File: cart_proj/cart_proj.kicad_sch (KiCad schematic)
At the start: 11 parts, among them CON1 GENESIS-EDGE, J1 PAD3, J2 PAD4, U1 PAL16R4, U2 74LS244, U3 74LS244, U4 GAME ROM

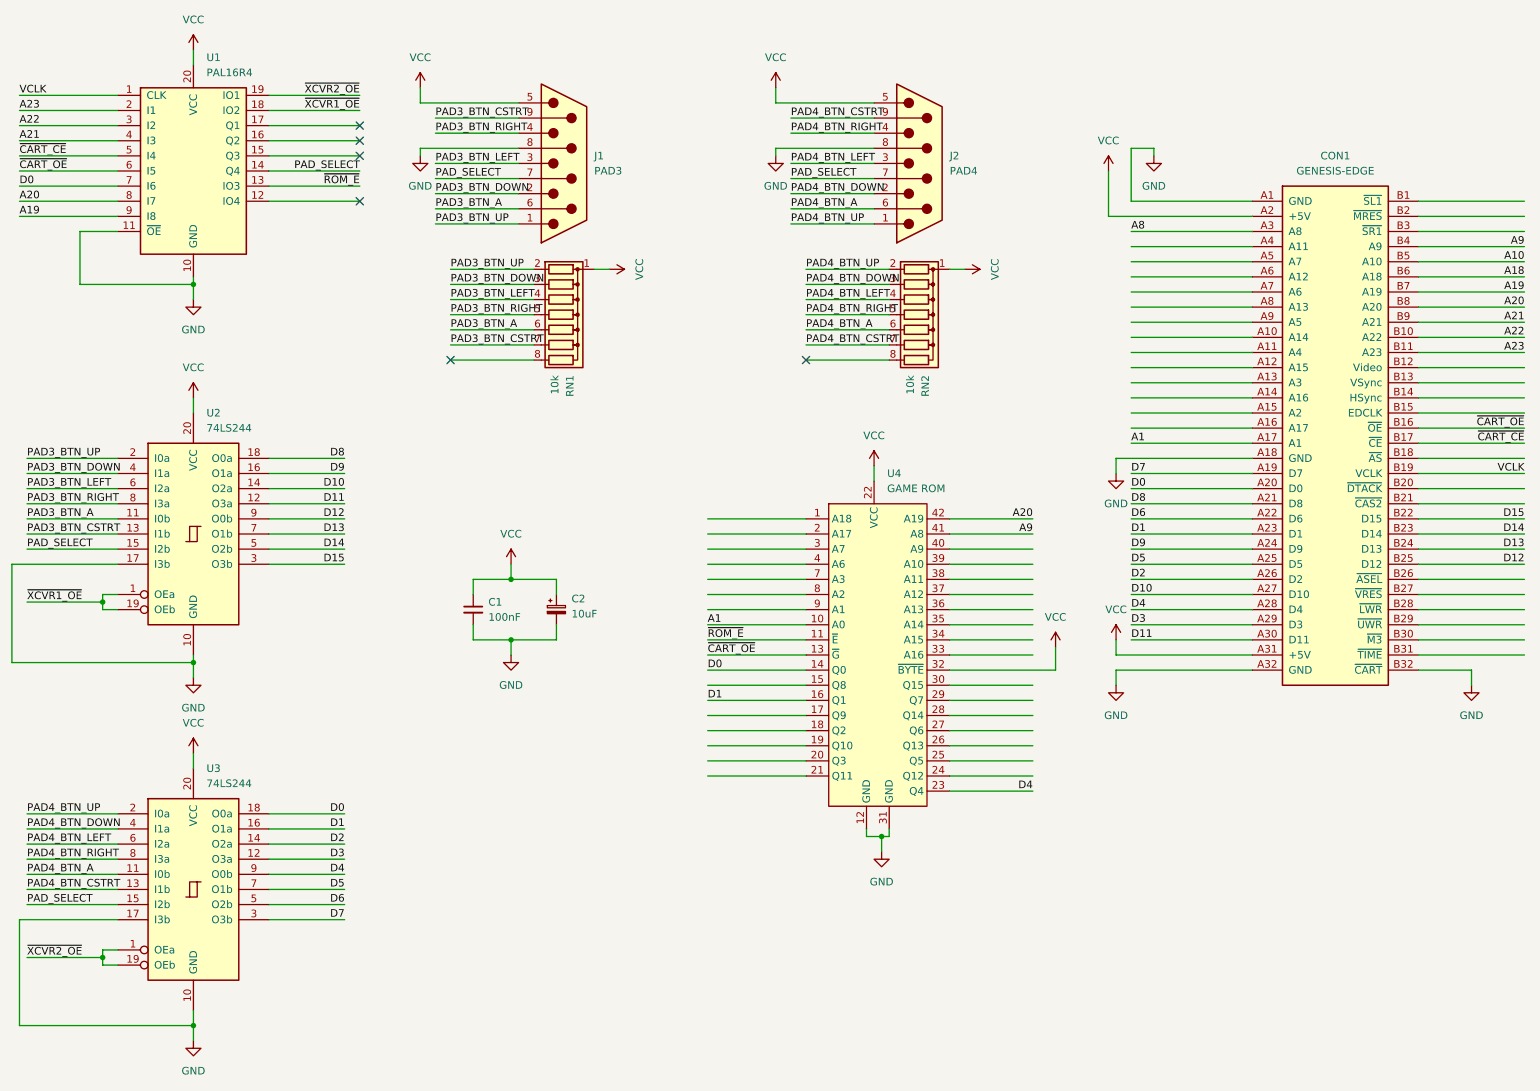
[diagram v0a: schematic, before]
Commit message: Update schematic, add pdf
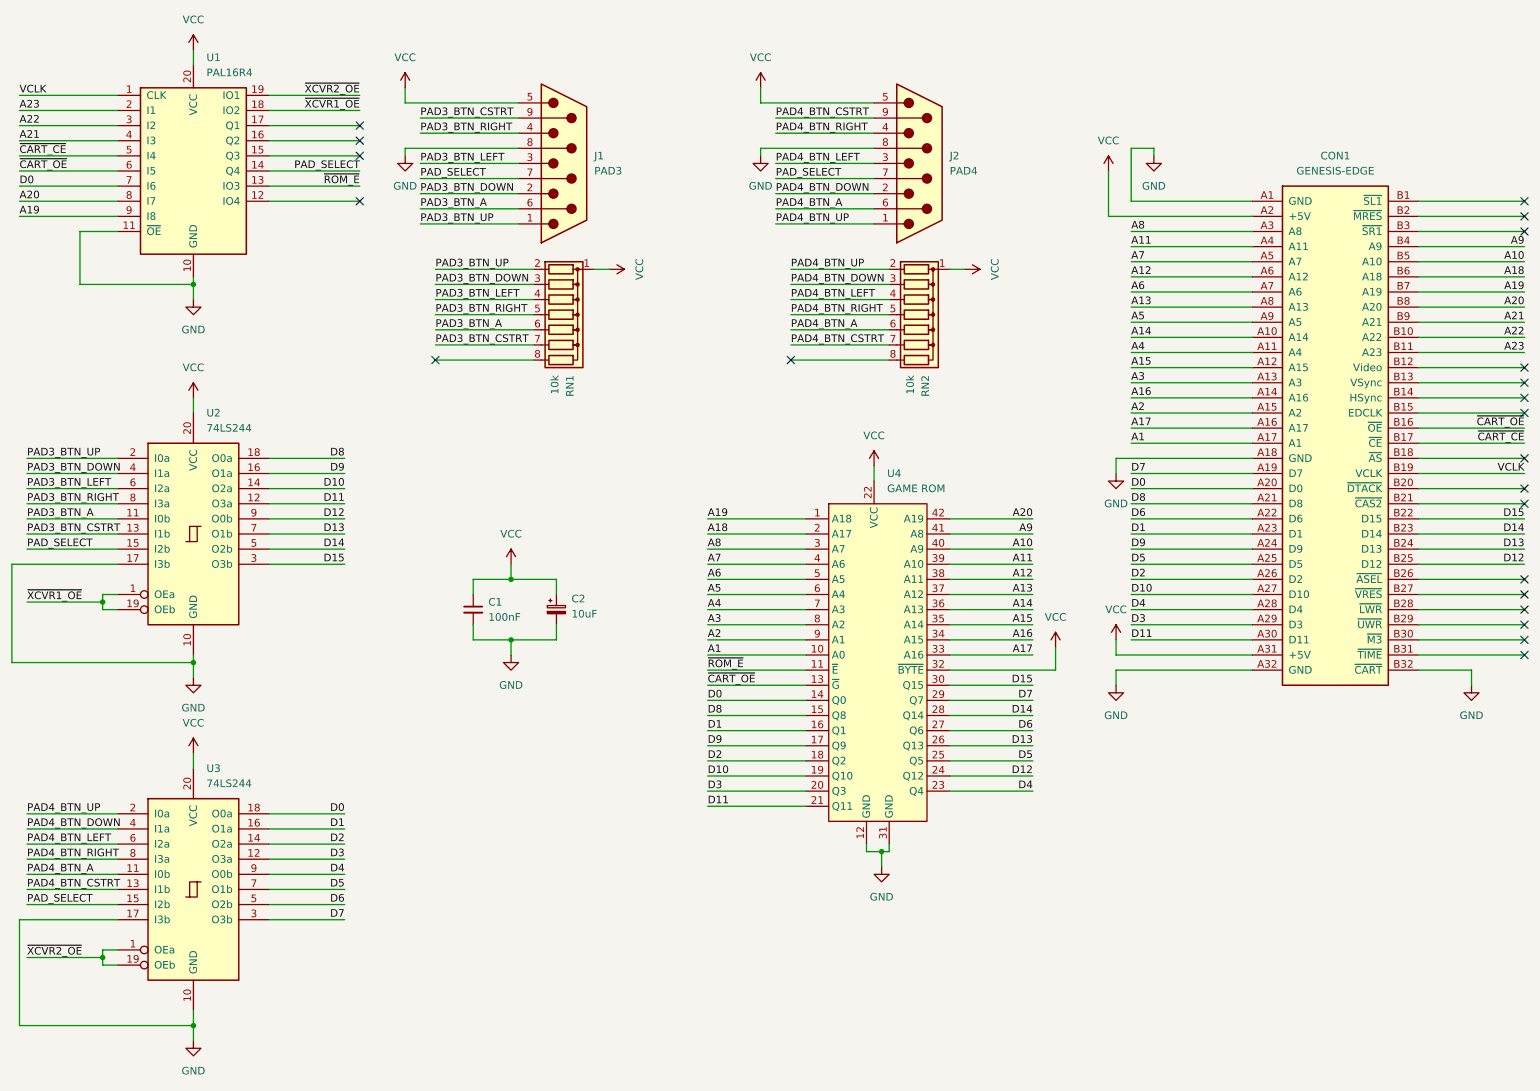
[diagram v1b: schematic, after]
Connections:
- net A10: now also U4.40 (A9)
- net A18: now also U4.2 (A17)
- net A19: now also U4.1 (A18)
- net A8: now also U4.3 (A7)
- net D10: now also U4.19 (Q10)
- net D11: now also U4.21 (Q11)
- net D12: now also U4.24 (Q12)
- net D13: now also U4.26 (Q13)
- net D14: now also U4.28 (Q14)
- net D15: now also U4.30 (Q15)
- net D2: now also U4.18 (Q2)
- net D3: now also U4.20 (Q3)
- net D5: now also U4.25 (Q5)
- net D6: now also U4.27 (Q6)
- net D7: now also U4.29 (Q7)
- net D8: now also U4.15 (Q8)
- net D9: now also U4.17 (Q9)
- net A17: now reaches U4.33 (A16)
- net A17: now also CON1.A16 (A17)
- net A16: now reaches U4.34 (A15)
- net A16: now also CON1.A14 (A16)
- net A15: now reaches U4.35 (A14)
- net A15: now also CON1.A12 (A15)
- net A14: now reaches U4.36 (A13)
- net A14: now also CON1.A10 (A14)
- net A13: now reaches U4.37 (A12)
- net A13: now also CON1.A8 (A13)
- net A12: now reaches U4.38 (A11)
- net A12: now also CON1.A6 (A12)
- net A11: now reaches U4.39 (A10)
- net A11: now also CON1.A4 (A11)
- net A7: now reaches U4.4 (A6)
- net A7: now also CON1.A5 (A7)
- net A4: now reaches U4.7 (A3)
- net A4: now also CON1.A11 (A4)
- net A3: now reaches U4.8 (A2)
- net A3: now also CON1.A13 (A3)
- net A2: now reaches U4.9 (A1)
- net A2: now also CON1.A15 (A2)
- net A6: now reaches CON1.A7 (A6)
- net A6: now also U4.5 (A5)
- net A5: now reaches CON1.A9 (A5)
- net A5: now also U4.6 (A4)
- no-connect marks 6 -> 22
